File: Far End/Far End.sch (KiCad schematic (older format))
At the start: 8 parts

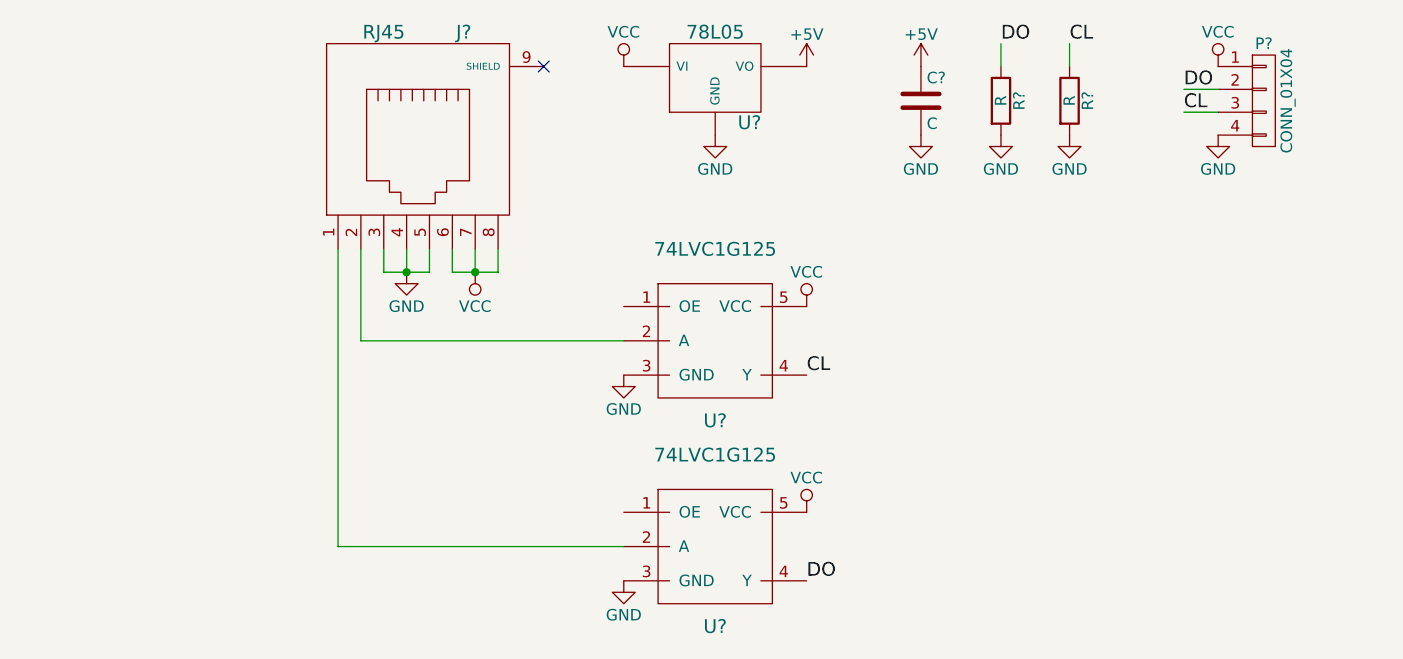
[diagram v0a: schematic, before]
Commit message: Far End properly ground twisted
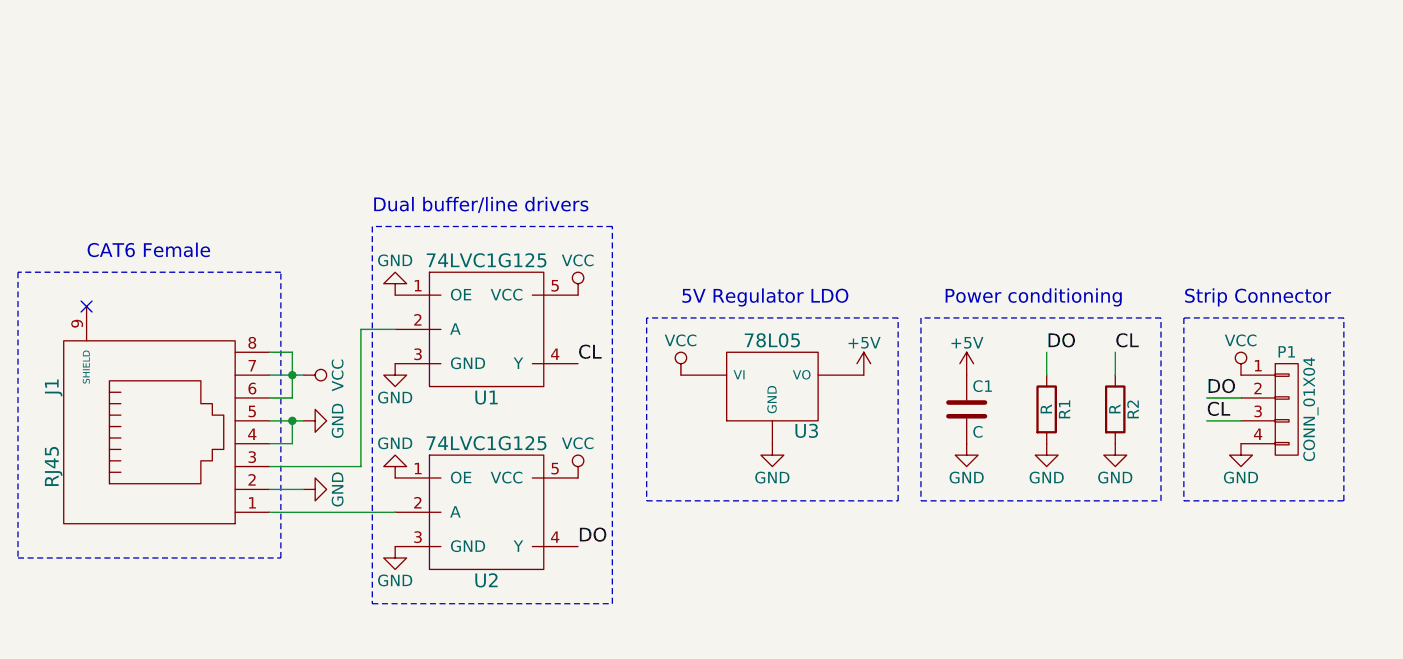
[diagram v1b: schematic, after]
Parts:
- C1: renamed from C?; footprint (none) -> Capacitors_SMD:C_0805
- J1: renamed from J?; footprint (none) -> Connect:RJ45_8
- P1: renamed from P?; footprint (none) -> Pin_Headers:Pin_Header_Straight_1x04
- R1, R2: renamed from R?; footprint (none) -> Resistors_SMD:R_0805
- U1, U2: renamed from U?; footprint (none) -> SMD_Packages:SOT-353
- U3: renamed from U?; footprint (none) -> Housings_SOT-89:SOT89-3_Housing
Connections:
- net GND: now also J1.2, U1.1 (OE), U2.1 (OE); no longer J1.3
- net at U1.2 (A): now also J1.3; no longer J1.2
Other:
- note added: "5V Regulator LDO"
- note added: "CAT6 Female"
- note added: "Dual buffer/line drivers"
- note added: "Power conditioning"
- note added: "Strip Connector"
- moved on the sheet: C1, J1, P1, R1, R2, U1, U2, U3
